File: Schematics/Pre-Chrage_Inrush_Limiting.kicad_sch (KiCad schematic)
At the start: 12 parts, among them J28 43650-0418, J7 464379202, J8 464369202, Q1 STB10NK60ZT4

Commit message: WIP PCB, Added Test Points, added icon file
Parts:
- renumbered D7 to D1, J28 to J7, J7 to J8, J8 to J9, R48 to R1, R1 to R2, R2 to R3, R3 to R4, TP55 to TP7, TP7 to TP8, TP8 to TP9
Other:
- moved on the sheet: TP7, TP8
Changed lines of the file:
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@@
 		(on_board yes)
 		(dnp no)
-		(property "Reference" "J8"
+		(property "Reference" "J9"
 			(at 259.08 49.276 0)
 			(effects
@@
 			(project "SiC_Single_Phase_Inverter"
 				(path "/a1ed0539-9735-4ad1-a8fd-87e26e7fce16/2ce2cec5-32d3-4a43-a037-f5e3105f4dec"
-					(reference "J8")
+					(reference "J9")
 					(unit 1)
 				)
@@
 		(on_board yes)
 		(dnp no)
-		(property "Reference" "R2"
+		(property "Reference" "R3"
 			(at 200.914 82.55 0)
 			(effects
@@
 			(project "SiC_Single_Phase_Inverter"
 				(path "/a1ed0539-9735-4ad1-a8fd-87e26e7fce16/2ce2cec5-32d3-4a43-a037-f5e3105f4dec"
-					(reference "R2")
+					(reference "R3")
 					(unit 1)
 				)
@@
 		(on_board yes)
 		(dnp no)
-		(property "Reference" "TP8"
+		(property "Reference" "TP9"
 			(at 246.126 93.472 0)
 			(effects
@@
 			(project "SiC_Single_Phase_Inverter"
 				(path "/a1ed0539-9735-4ad1-a8fd-87e26e7fce16/2ce2cec5-32d3-4a43-a037-f5e3105f4dec"
-					(reference "TP8")
+					(reference "TP9")
 					(unit 1)
 				)
@@
 		(on_board yes)
 		(dnp no)
-		(property "Reference" "R48"
+		(property "Reference" "R1"
 			(at 184.15 74.93 0)
 			(effects
@@
 			(project "SiC_Single_Phase_Inverter"
 				(path "/a1ed0539-9735-4ad1-a8fd-87e26e7fce16/2ce2cec5-32d3-4a43-a037-f5e3105f4dec"
-					(reference "R48")
+					(reference "R1")
 					(unit 1)
 				)
@@
 		(dnp no)
 		(fields_autoplaced yes)
-		(property "Reference" "D7"
+		(property "Reference" "D1"
 			(at 209.55 72.3899 90)
 			(effects
@@
 			(project "SiC_Single_Phase_Inverter"
 				(path "/a1ed0539-9735-4ad1-a8fd-87e26e7fce16/2ce2cec5-32d3-4a43-a037-f5e3105f4dec"
-					(reference "D7")
+					(reference "D1")
 					(unit 1)
 				)
@@
 		(dnp no)
 		(fields_autoplaced yes)
-		(property "Reference" "#PWR06"
+		(property "Reference" "#PWR07"
 			(at 241.3 104.14 0)
 			(effects
@@
 			(project "SiC_Single_Phase_Inverter"
 				(path "/a1ed0539-9735-4ad1-a8fd-87e26e7fce16/2ce2cec5-32d3-4a43-a037-f5e3105f4dec"
-					(reference "#PWR06")
+					(reference "#PWR07")
 					(unit 1)
 				)
@@
 		(dnp no)
 		(fields_autoplaced yes)
-		(property "Reference" "#PWR0149"
+		(property "Reference" "#PWR05"
 			(at 139.7 137.16 0)
 			(effects
@@
 			(project "SiC_Single_Phase_Inverter"
 				(path "/a1ed0539-9735-4ad1-a8fd-87e26e7fce16/2ce2cec5-32d3-4a43-a037-f5e3105f4dec"
-					(reference "#PWR0149")
+					(reference "#PWR05")
 					(unit 1)
 				)
@@
 		(on_board yes)
 		(dnp no)
-		(property "Reference" "R3"
+		(property "Reference" "R4"
 			(at 200.914 92.71 0)
 			(effects
@@
 			(project "SiC_Single_Phase_Inverter"
 				(path "/a1ed0539-9735-4ad1-a8fd-87e26e7fce16/2ce2cec5-32d3-4a43-a037-f5e3105f4dec"
-					(reference "R3")
+					(reference "R4")
 					(unit 1)
 				)
@@
 		(dnp no)
 		(fields_autoplaced yes)
-		(property "Reference" "J7"
+		(property "Reference" "J8"
 			(at 151.13 45.72 0)
 			(effects
@@
 			(project "SiC_Single_Phase_Inverter"
 				(path "/a1ed0539-9735-4ad1-a8fd-87e26e7fce16/2ce2cec5-32d3-4a43-a037-f5e3105f4dec"
-					(reference "J7")
+					(reference "J8")
 					(unit 1)
 				)
@@
 		(dnp no)
 		(fields_autoplaced yes)
-		(property "Reference" "#PWR05"
+		(property "Reference" "#PWR06"
 			(at 166.37 99.06 0)
 			(effects
@@
 			(project "SiC_Single_Phase_Inverter"
 				(path "/a1ed0539-9735-4ad1-a8fd-87e26e7fce16/2ce2cec5-32d3-4a43-a037-f5e3105f4dec"
-					(reference "#PWR05")
+					(reference "#PWR06")
 					(unit 1)
 				)
@@
 		(dnp no)
 		(fields_autoplaced yes)
-		(property "Reference" "R1"
+		(property "Reference" "R2"
 			(at 199.39 49.53 90)
 			(effects
@@
 			(project ""
 				(path "/a1ed0539-9735-4ad1-a8fd-87e26e7fce16/2ce2cec5-32d3-4a43-a037-f5e3105f4dec"
-					(reference "R1")
+					(reference "R2")
 					(unit 1)
 				)
@@
 	(symbol
 		(lib_id "SiC_Inverter:5277")
-		(at 204.47 90.17 0)
-		(unit 1)
-		(exclude_from_sim no)
-		(in_bom yes)
-		(on_board yes)
-		(dnp no)
-		(property "Reference" "TP55"
-			(at 210.058 87.122 0)
+		(at 204.47 91.44 0)
+		(unit 1)
+		(exclude_from_sim no)
+		(in_bom yes)
+		(on_board yes)
+		(dnp no)
+		(property "Reference" "TP7"
+			(at 210.058 88.392 0)
 			(effects
 				(font
@@
 		)
 		(property "Value" "5277"
-			(at 188.468 103.124 0)
+			(at 188.468 104.394 0)
 			(effects
 				(font
@@
 		)
 		(property "Footprint" "SiC_Inverter:5277"
-			(at 194.564 101.346 0)
+			(at 194.564 102.616 0)
 			(effects
 				(font
@@
 		)
 		(property "Datasheet" "https://www.keyelco.com/userAssets/file/K75p62.pdf"
-			(at 212.344 97.536 0)
+			(at 212.344 98.806 0)
 			(effects
 				(font
@@
 		)
 		(property "Description" "Test Plugs & Test Jacks TEST POINT (BLUE) - COMPACT"
-			(at 214.884 99.568 0)
-			(effects
-				(font
-					(size 1.27 1.27)
-				)
-				(hide yes)
-			)
-		)
-		(pin "1"
-		)
-		(instances
-			(project "SiC_Single_Phase_Inverter"
-				(path "/a1ed0539-9735-4ad1-a8fd-87e26e7fce16/2ce2cec5-32d3-4a43-a037-f5e3105f4dec"
-					(reference "TP55")
+			(at 214.884 100.838 0)
+			(effects
+				(font
+					(size 1.27 1.27)
+				)
+				(hide yes)
+			)
+		)
+		(pin "1"
+		)
+		(instances
+			(project "SiC_Single_Phase_Inverter"
+				(path "/a1ed0539-9735-4ad1-a8fd-87e26e7fce16/2ce2cec5-32d3-4a43-a037-f5e3105f4dec"
+					(reference "TP7")
 					(unit 1)
 				)
@@
 	(symbol
 		(lib_id "SiC_Inverter:5277")
-		(at 245.11 60.96 180)
-		(unit 1)
-		(exclude_from_sim no)
-		(in_bom yes)
-		(on_board yes)
-		(dnp no)
-		(property "Reference" "TP7"
-			(at 244.094 64.008 0)
+		(at 245.11 59.69 180)
+		(unit 1)
+		(exclude_from_sim no)
+		(in_bom yes)
+		(on_board yes)
+		(dnp no)
+		(property "Reference" "TP8"
+			(at 244.094 62.738 0)
 			(effects
 				(font
@@
 		)
 		(property "Value" "5277"
-			(at 261.112 48.006 0)
+			(at 261.112 46.736 0)
 			(effects
 				(font
@@
 		)
 		(property "Footprint" "SiC_Inverter:5277"
-			(at 255.016 49.784 0)
+			(at 255.016 48.514 0)
 			(effects
 				(font
@@
 		)
 		(property "Datasheet" "https://www.keyelco.com/userAssets/file/K75p62.pdf"
-			(at 237.236 53.594 0)
+			(at 237.236 52.324 0)
 			(effects
 				(font
@@
 		)
 		(property "Description" "Test Plugs & Test Jacks TEST POINT (BLUE) - COMPACT"
-			(at 234.696 51.562 0)
-			(effects
-				(font
-					(size 1.27 1.27)
-				)
-				(hide yes)
-			)
-		)
-		(pin "1"
-		)
-		(instances
-			(project "SiC_Single_Phase_Inverter"
-				(path "/a1ed0539-9735-4ad1-a8fd-87e26e7fce16/2ce2cec5-32d3-4a43-a037-f5e3105f4dec"
-					(reference "TP7")
+			(at 234.696 50.292 0)
+			(effects
+				(font
+					(size 1.27 1.27)
+				)
+				(hide yes)
+			)
+		)
+		(pin "1"
+		)
+		(instances
+			(project "SiC_Single_Phase_Inverter"
+				(path "/a1ed0539-9735-4ad1-a8fd-87e26e7fce16/2ce2cec5-32d3-4a43-a037-f5e3105f4dec"
+					(reference "TP8")
 					(unit 1)
 				)
@@
 		(dnp no)
 		(fields_autoplaced yes)
-		(property "Reference" "J28"
+		(property "Reference" "J7"
 			(at 161.29 125.3489 0)
 			(effects
@@
 			(project "SiC_Single_Phase_Inverter"
 				(path "/a1ed0539-9735-4ad1-a8fd-87e26e7fce16/2ce2cec5-32d3-4a43-a037-f5e3105f4dec"
-					(reference "J28")
-					(unit 1)
-				)
+					(reference "J7")
+					(unit 1)
+				)

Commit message: WIP PCB Design
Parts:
- added H13, H14, H15, H16: MountingHole, MountingHole:MountingHole_2.2mm_M2, symbol Mechanical:MountingHole

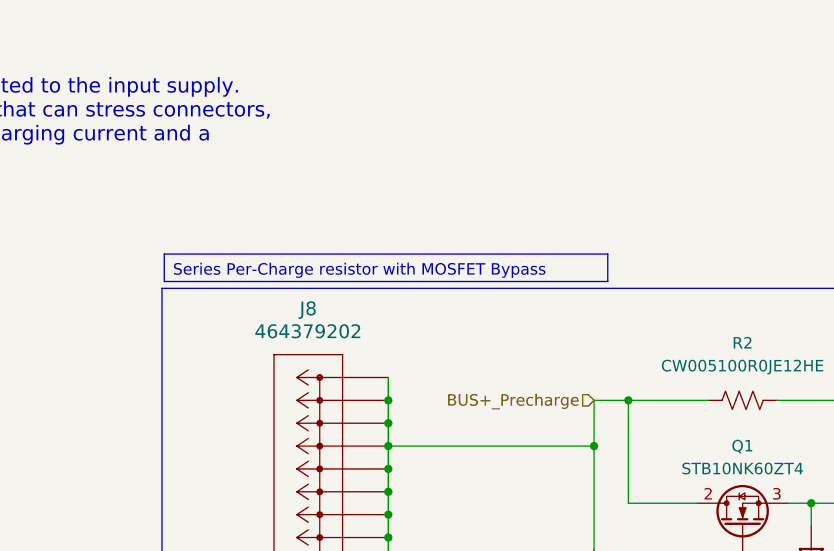
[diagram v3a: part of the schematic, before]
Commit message: Adding Damping Resiter to AC Output Filter and mounting points
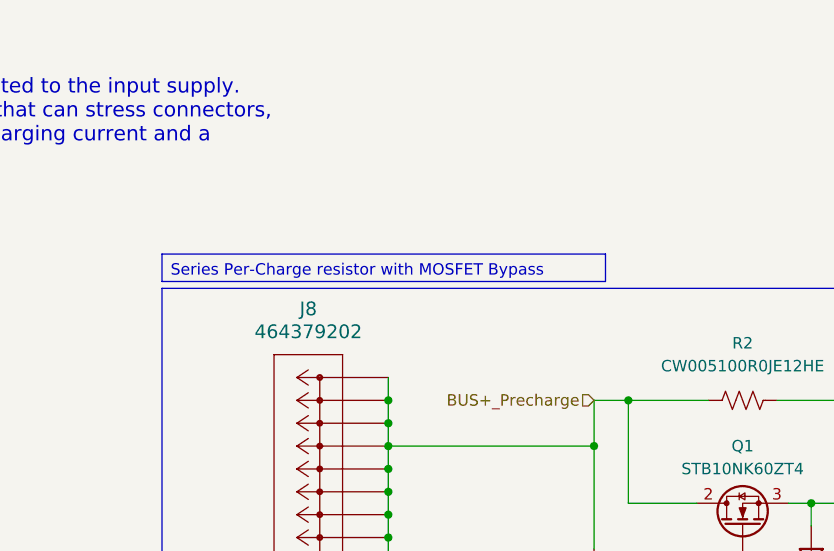
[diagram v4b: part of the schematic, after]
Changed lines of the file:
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@@
 	(text_box "Series Per-Charge resistor with MOSFET Bypass"
 		(exclude_from_sim no)
-		(at 135.128 39.624 0)
+		(at 134.874 39.624 0)
 		(size 49.276 3.048)
 		(margins 0.9525 0.9525 0.9525 0.9525)
